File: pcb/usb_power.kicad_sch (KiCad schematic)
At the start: 3 parts, among them J1 USB_C_Receptacle_USB2.0, J3 Jack-DC

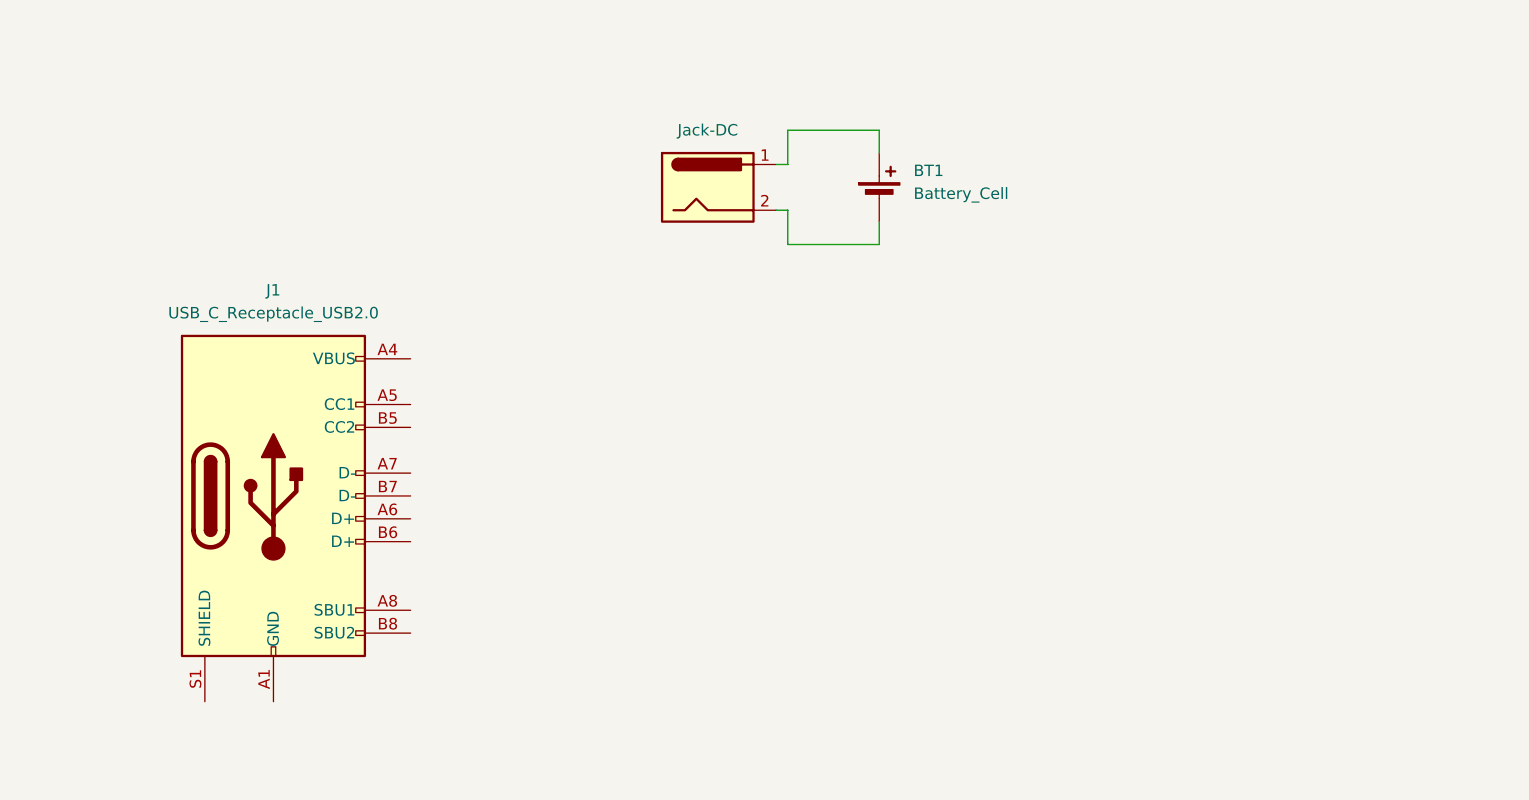
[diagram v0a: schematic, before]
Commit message: Adicionando Regulador AMS117-3.3
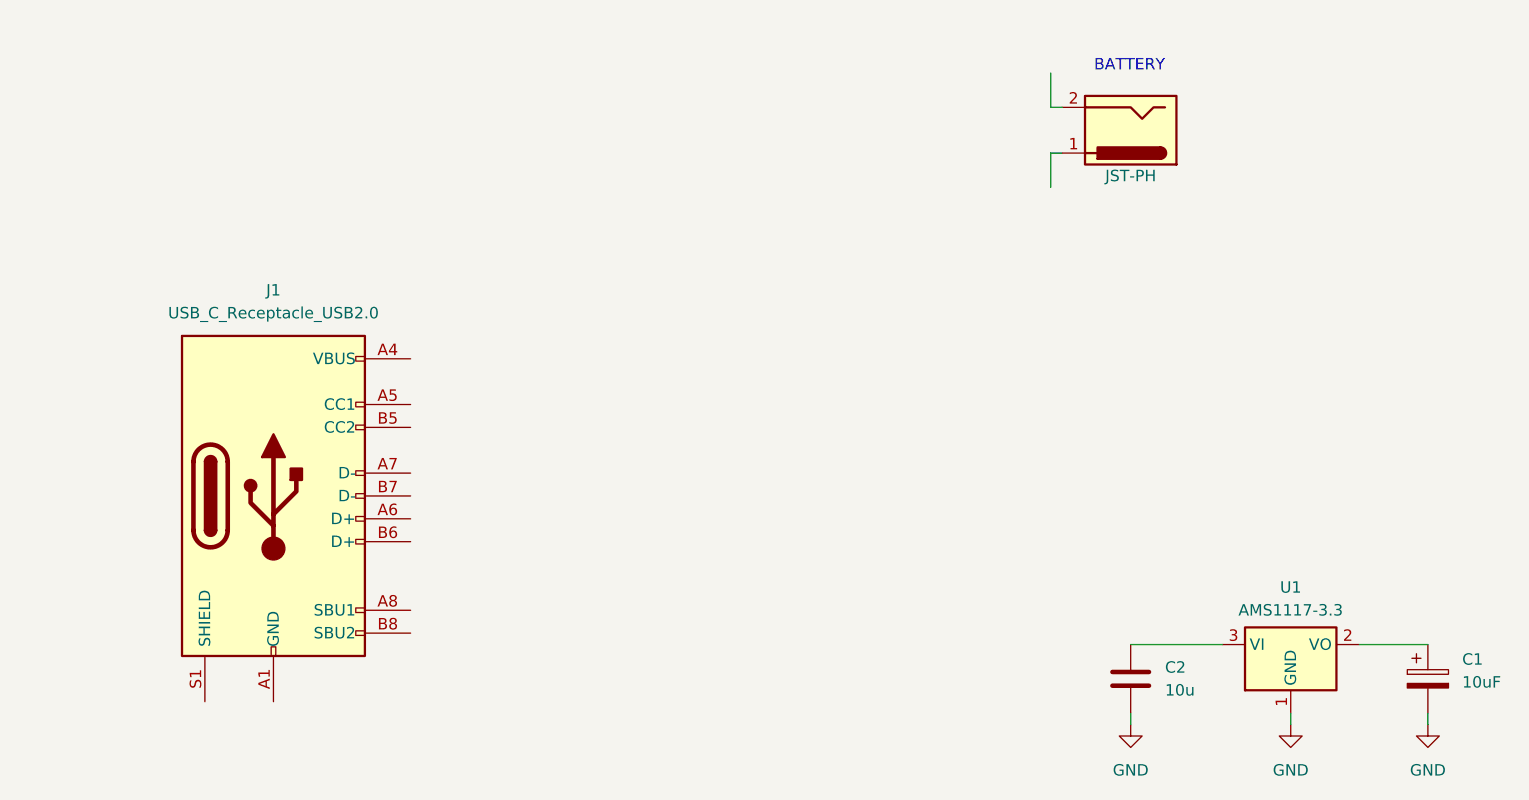
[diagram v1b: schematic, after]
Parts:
- removed BT1: Battery_Cell, symbol Device:Battery_Cell
- added C1: 10uF, symbol Device:C_Polarized
- added C2: 10u, symbol Device:C
- added U1: AMS1117-3.3, Package_TO_SOT_SMD:SOT-223-3_TabPin2, symbol Regulator_Linear:AMS1117-3.3
- J3: value Jack-DC -> JST-PH
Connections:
- new net: C2.1, U1.3 (VI)
- new net: C1.1, U1.2 (VO)
- new net GND: C1.2, C2.2, U1.1 (GND)
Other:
- note added: "BATTERY"
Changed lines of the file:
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@@
 (kicad_sch (version 20230121) (generator eeschema)
   (paper "A4")
-  (wire (pts (xy 125.73 40.64) (xy 125.73 36.83))
-    (stroke (width 0) (type default))
-  )
-  (wire (pts (xy 124.46 45.72) (xy 125.73 45.72))
-    (stroke (width 0) (type default))
-  )
-  (wire (pts (xy 135.89 36.83) (xy 135.89 39.37))
-    (stroke (width 0) (type default))
-  )
-  (wire (pts (xy 125.73 49.53) (xy 135.89 49.53))
-    (stroke (width 0) (type default))
-  )
-  (wire (pts (xy 135.89 46.99) (xy 135.89 49.53))
-    (stroke (width 0) (type default))
-  )
-  (wire (pts (xy 124.46 40.64) (xy 125.73 40.64))
-    (stroke (width 0) (type default))
-  )
-  (wire (pts (xy 125.73 45.72) (xy 125.73 49.53))
-    (stroke (width 0) (type default))
-  )
-  (wire (pts (xy 125.73 36.83) (xy 135.89 36.83))
-    (stroke (width 0) (type default))
-  )
-  (symbol (lib_id "Connector:Jack-DC") (at 116.84 43.18 0) (unit 1)
-    (in_bom yes) (on_board yes) (dnp no) (fields_autoplaced)
-    (property "Reference" "J3" (at 116.84 34.29 0)
-      (effects (font (size 1.27 1.27)) hide)
-    )
-    (property "Value" "Jack-DC" (at 116.84 36.83 0)
-      (effects (font (size 1.27 1.27)))
-    )
-    (property "Footprint" "" (at 118.11 44.196 0)
-      (effects (font (size 1.27 1.27)) hide)
-    )
-    (property "Datasheet" "~" (at 118.11 44.196 0)
+  (wire (pts (xy 154.94 39.37) (xy 154.94 43.18))
+    (stroke (width 0) (type default))
+  )
+  (wire (pts (xy 156.21 34.29) (xy 154.94 34.29))
+    (stroke (width 0) (type default))
+  )
+  (wire (pts (xy 163.83 93.98) (xy 173.99 93.98))
+    (stroke (width 0) (type default))
+  )
+  (wire (pts (xy 181.61 101.6) (xy 181.61 102.87))
+    (stroke (width 0) (type default))
+  )
+  (wire (pts (xy 156.21 39.37) (xy 154.94 39.37))
+    (stroke (width 0) (type default))
+  )
+  (wire (pts (xy 189.23 93.98) (xy 196.85 93.98))
+    (stroke (width 0) (type default))
+  )
+  (wire (pts (xy 196.85 101.6) (xy 196.85 102.87))
+    (stroke (width 0) (type default))
+  )
+  (wire (pts (xy 154.94 34.29) (xy 154.94 30.48))
+    (stroke (width 0) (type default))
+  )
+  (wire (pts (xy 163.83 101.6) (xy 163.83 102.87))
+    (stroke (width 0) (type default))
+  )
+  (text "BATTERY" (at 167.64 30.48 0)
+    (effects (font (size 1.27 1.27)) (justify right bottom))
+  )
+  (symbol (lib_id "Connector:Jack-DC") (at 163.83 36.83 180) (unit 1)
+    (in_bom yes) (on_board yes) (dnp no)
+    (property "Reference" "J3" (at 163.83 45.72 0)
+      (effects (font (size 1.27 1.27)) hide)
+    )
+    (property "Value" "JST-PH" (at 163.83 41.91 0)
+      (effects (font (size 1.27 1.27)))
+    )
+    (property "Footprint" "" (at 162.56 35.814 0)
+      (effects (font (size 1.27 1.27)) hide)
+    )
+    (property "Datasheet" "~" (at 162.56 35.814 0)
       (effects (font (size 1.27 1.27)) hide)
     )
@@
         (path "/e186517a-3325-4e77-9fb6-41adae966a58/608b05ec-cb35-4972-81cc-6671fc638f48"
           (reference "J3") (unit 1)
+        )
+      )
+    )
+  )
+  (symbol (lib_id "Device:C") (at 163.83 97.79 0) (unit 1)
+    (in_bom yes) (on_board yes) (dnp no) (fields_autoplaced)
+    (property "Reference" "C2" (at 167.64 96.52 0)
+      (effects (font (size 1.27 1.27)) (justify left))
+    )
+    (property "Value" "10u" (at 167.64 99.06 0)
+      (effects (font (size 1.27 1.27)) (justify left))
+    )
+    (property "Footprint" "" (at 164.7952 101.6 0)
+      (effects (font (size 1.27 1.27)) hide)
+    )
+    (property "Datasheet" "~" (at 163.83 97.79 0)
+      (effects (font (size 1.27 1.27)) hide)
+    )
+    (pin "2")
+    (pin "1")
+    (instances
+      (project "lily58_keyboard"
+        (path "/e186517a-3325-4e77-9fb6-41adae966a58/608b05ec-cb35-4972-81cc-6671fc638f48"
+          (reference "C2") (unit 1)
+        )
+      )
+    )
+  )
+  (symbol (lib_id "power:GND") (at 181.61 102.87 0) (unit 1)
+    (in_bom yes) (on_board yes) (dnp no) (fields_autoplaced)
+    (property "Reference" "#PWR02" (at 181.61 109.22 0)
+      (effects (font (size 1.27 1.27)) hide)
+    )
+    (property "Value" "GND" (at 181.61 107.95 0)
+      (effects (font (size 1.27 1.27)))
+    )
+    (property "Footprint" "" (at 181.61 102.87 0)
+      (effects (font (size 1.27 1.27)) hide)
+    )
+    (property "Datasheet" "" (at 181.61 102.87 0)
+      (effects (font (size 1.27 1.27)) hide)
+    )
+    (pin "1")
+    (instances
+      (project "lily58_keyboard"
+        (path "/e186517a-3325-4e77-9fb6-41adae966a58/608b05ec-cb35-4972-81cc-6671fc638f48"
+          (reference "#PWR02") (unit 1)
+        )
+      )
+    )
+  )
+  (symbol (lib_id "power:GND") (at 196.85 102.87 0) (unit 1)
+    (in_bom yes) (on_board yes) (dnp no) (fields_autoplaced)
+    (property "Reference" "#PWR03" (at 196.85 109.22 0)
+      (effects (font (size 1.27 1.27)) hide)
+    )
+    (property "Value" "GND" (at 196.85 107.95 0)
+      (effects (font (size 1.27 1.27)))
+    )
+    (property "Footprint" "" (at 196.85 102.87 0)
+      (effects (font (size 1.27 1.27)) hide)
+    )
+    (property "Datasheet" "" (at 196.85 102.87 0)
+      (effects (font (size 1.27 1.27)) hide)
+    )
+    (pin "1")
+    (instances
+      (project "lily58_keyboard"
+        (path "/e186517a-3325-4e77-9fb6-41adae966a58/608b05ec-cb35-4972-81cc-6671fc638f48"
+          (reference "#PWR03") (unit 1)
+        )
+      )
+    )
+  )
+  (symbol (lib_id "power:GND") (at 163.83 102.87 0) (unit 1)
+    (in_bom yes) (on_board yes) (dnp no) (fields_autoplaced)
+    (property "Reference" "#PWR01" (at 163.83 109.22 0)
+      (effects (font (size 1.27 1.27)) hide)
+    )
+    (property "Value" "GND" (at 163.83 107.95 0)
+      (effects (font (size 1.27 1.27)))
+    )
+    (property "Footprint" "" (at 163.83 102.87 0)
+      (effects (font (size 1.27 1.27)) hide)
+    )
+    (property "Datasheet" "" (at 163.83 102.87 0)
+      (effects (font (size 1.27 1.27)) hide)
+    )
+    (pin "1")
+    (instances
+      (project "lily58_keyboard"
+        (path "/e186517a-3325-4e77-9fb6-41adae966a58/608b05ec-cb35-4972-81cc-6671fc638f48"
+          (reference "#PWR01") (unit 1)
         )
       )
@@
     )
   )
-  (symbol (lib_id "Device:Battery_Cell") (at 135.89 44.45 0) (unit 1)
-    (in_bom yes) (on_board yes) (dnp no) (fields_autoplaced)
-    (property "Reference" "BT1" (at 139.7 41.3385 0)
-      (effects (font (size 1.27 1.27)) (justify left))
-    )
-    (property "Value" "Battery_Cell" (at 139.7 43.8785 0)
-      (effects (font (size 1.27 1.27)) (justify left))
-    )
-    (property "Footprint" "" (at 135.89 42.926 90)
-      (effects (font (size 1.27 1.27)) hide)
-    )
-    (property "Datasheet" "~" (at 135.89 42.926 90)
-      (effects (font (size 1.27 1.27)) hide)
-    )
-    (pin "2")
-    (pin "1")
-    (instances
-      (project "lily58_keyboard"
-        (path "/e186517a-3325-4e77-9fb6-41adae966a58/608b05ec-cb35-4972-81cc-6671fc638f48"
-          (reference "BT1") (unit 1)
-        )
-      )
+  (symbol (lib_id "Device:C_Polarized") (at 196.85 97.79 0) (unit 1)
+    (in_bom yes) (on_board yes) (dnp no) (fields_autoplaced)
+    (property "Reference" "C1" (at 200.66 95.631 0)
+      (effects (font (size 1.27 1.27)) (justify left))
+    )
+    (property "Value" "10uF" (at 200.66 98.171 0)
+      (effects (font (size 1.27 1.27)) (justify left))
+    )
+    (property "Footprint" "" (at 197.8152 101.6 0)
+      (effects (font (size 1.27 1.27)) hide)
+    )
+    (property "Datasheet" "~" (at 196.85 97.79 0)
+      (effects (font (size 1.27 1.27)) hide)
+    )
+    (pin "2")
+    (pin "1")
+    (instances
+      (project "lily58_keyboard"
+        (path "/e186517a-3325-4e77-9fb6-41adae966a58/608b05ec-cb35-4972-81cc-6671fc638f48"
+          (reference "C1") (unit 1)
+        )
+      )
+    )
+  )
+  (symbol (lib_id "Regulator_Linear:AMS1117-3.3") (at 181.61 93.98 0) (unit 1)
+    (in_bom yes) (on_board yes) (dnp no) (fields_autoplaced)
+    (property "Reference" "U1" (at 181.61 87.63 0)
+      (effects (font (size 1.27 1.27)))
+    )
+    (property "Value" "AMS1117-3.3" (at 181.61 90.17 0)
+      (effects (font (size 1.27 1.27)))
+    )
+    (property "Footprint" "Package_TO_SOT_SMD:SOT-223-3_TabPin2" (at 181.61 88.9 0)
+      (effects (font (size 1.27 1.27)) hide)
+    )
+    (property "Datasheet" "https://datasheet.lcsc.com/lcsc/2001081204_Shikues-AMS1117-1-2_C475600.pdf" (at 184.15 100.33 0)
+      (effects (font (size 1.27 1.27)) hide)
+    )
+    (pin "1")
+    (pin "2")
+    (pin "3")
+    (instances
+      (project "lily58_keyboard"
+        (path "/e186517a-3325-4e77-9fb6-41adae966a58/608b05ec-cb35-4972-81cc-6671fc638f48"
+          (reference "U1") (unit 1)
+        )
+      )

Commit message: USB 3.1 Type C com PD configurado
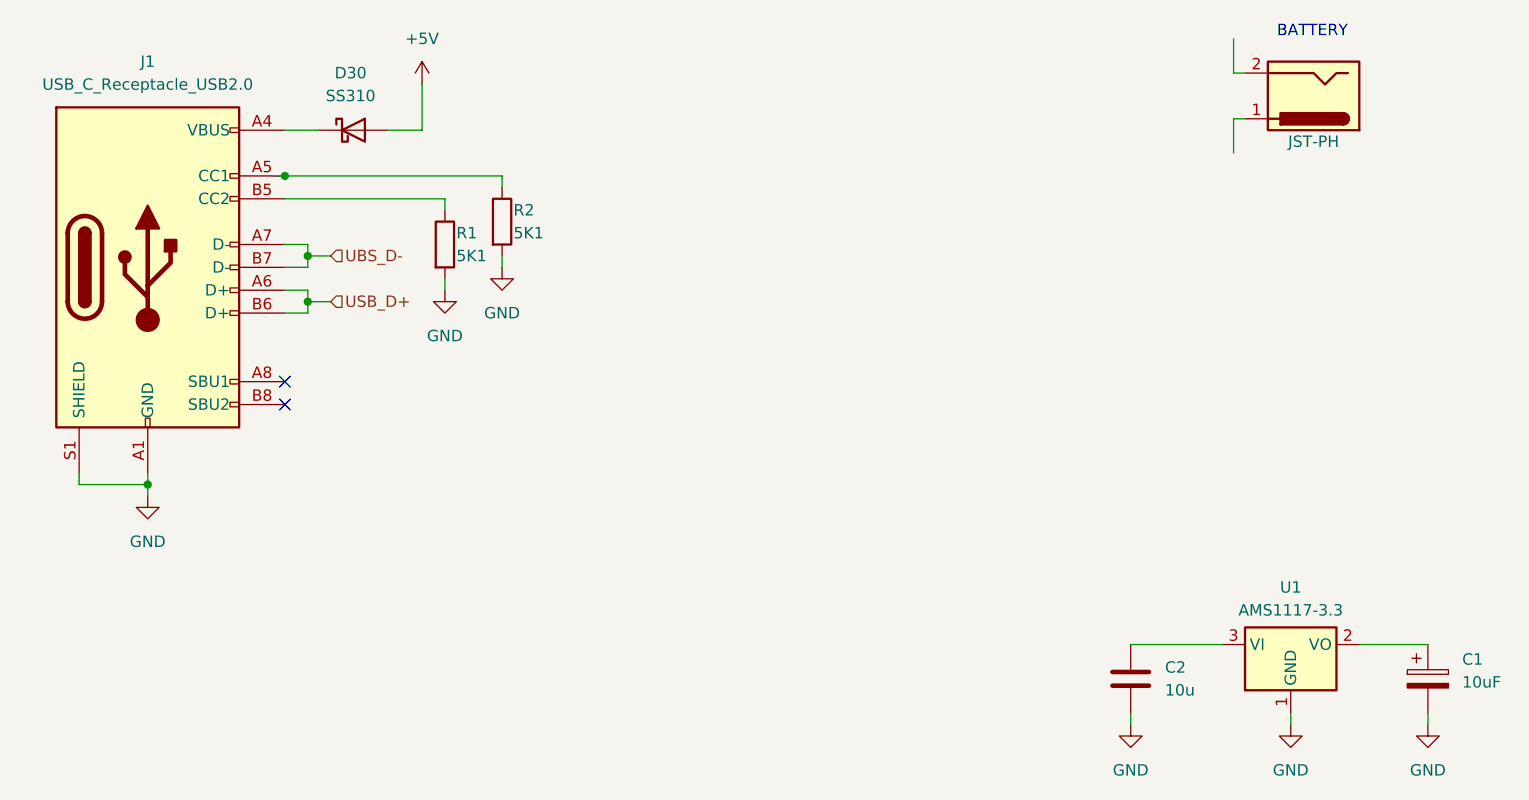
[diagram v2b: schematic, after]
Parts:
- added D30: SS310, symbol Device:D_Schottky
- added R1, R2: 5K1, symbol Device:R
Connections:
- net GND: now also J1.A1 (GND), J1.A12 (GND), J1.B1 (GND), J1.B12 (GND), J1.S1 (SHIELD), R1.2, R2.2
- net at J1.A4 (VBUS), J1.A9 (VBUS), J1.B4 (VBUS)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: now also D30.1 (K)
- net at J1.A5 (CC1): now also R2.1
- net USB_D+: now reaches J1.A6 (D+)
- net USB_D+: now also J1.B6 (D+)
- net UBS_D-: now reaches J1.A7 (D-)
- net UBS_D-: now also J1.B7 (D-)
- net at J1.B5 (CC2): now also R1.1
- new net +5V: D30.2 (A)
- no-connect marks 0 -> 2
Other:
- company: (none) -> Rich Mentality
- title: (none) -> バングー Keyboard Schematic
- moved on the sheet: J1
